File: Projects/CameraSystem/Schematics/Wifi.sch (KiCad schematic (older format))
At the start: 0 parts

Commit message: wifi module added
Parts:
- added C?: 100n, symbol Device:C
- added R?: 10k, symbol Device:R
- added U?: ESP8266, symbol cl-integrated_circuits:ESP8266
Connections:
- new net GND: C?.2, U?.1 (GND)
- new net VDD_3V3: C?.1, R?.1, U?.8 (3.3V)
- new net WIFI_EN: R?.2, U?.4 (CHEN)
- new net WIFI_RST: U?.6 (RST)
- new net WIFI_RX: U?.7 (RXI)
- new net WIFI_TX: U?.2 (TXO)
- no-connect marks 0 -> 2
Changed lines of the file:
@@
 Comment4 ""
 $EndDescr
+$Comp
+L cl-integrated_circuits:ESP8266 U?
+U 1 1 5CA59F23
+P 3450 2550
+F 0 "U?" H 3450 2987 60  0000 C CNN
+F 1 "ESP8266" H 3450 2881 60  0000 C CNN
+F 2 "" H 3450 2550 60  0001 C CNN
+F 3 "" H 3450 2550 60  0001 C CNN
+	1    3450 2550
+	1    0    0    -1
+$EndComp
+Text HLabel 4750 2700 2    50   Input ~ 0
+WIFI_RX
+Text HLabel 2450 2400 0    50   Output ~ 0
+WIFI_TX
+Text HLabel 2450 2700 0    50   Input ~ 0
+VDD_3V3
+Wire Wire Line
+	2450 2700 2750 2700
+Wire Wire Line
+	2950 2600 2450 2600
+Text HLabel 2450 2600 0    50   Input ~ 0
+WIFI_RST
+$Comp
+L power:GND #PWR?
+U 1 1 5CA5A1DA
+P 4700 2400
+F 0 "#PWR?" H 4700 2150 50  0001 C CNN
+F 1 "GND" V 4705 2272 50  0000 R CNN
+F 2 "" H 4700 2400 50  0001 C CNN
+F 3 "" H 4700 2400 50  0001 C CNN
+	1    4700 2400
+	0    -1   -1   0
+$EndComp
+Wire Wire Line
+	3950 2400 4700 2400
+Wire Wire Line
+	3950 2700 4750 2700
+Wire Wire Line
+	2450 2400 2950 2400
+NoConn ~ 3950 2500
+NoConn ~ 3950 2600
+Wire Wire Line
+	2950 2500 1900 2500
+Text HLabel 1750 2500 0    50   Input ~ 0
+WIFI_EN
+$Comp
+L Device:R R?
+U 1 1 5CA5A6FA
+P 1900 2200
+F 0 "R?" H 1970 2246 50  0000 L CNN
+F 1 "10k" H 1970 2155 50  0000 L CNN
+F 2 "" V 1830 2200 50  0001 C CNN
+F 3 "~" H 1900 2200 50  0001 C CNN
+	1    1900 2200
+	1    0    0    -1
+$EndComp
+Wire Wire Line
+	1900 2350 1900 2500
+Connection ~ 1900 2500
+Wire Wire Line
+	1900 2500 1750 2500
+Wire Wire Line
+	1900 2050 1900 1850
+Text Label 1900 1850 0    50   ~ 0
+VDD_3V3
+$Comp
+L Device:C C?
+U 1 1 5CA5ADFE
+P 2750 3000
+F 0 "C?" H 2865 3046 50  0000 L CNN
+F 1 "100n" H 2865 2955 50  0000 L CNN
+F 2 "" H 2788 2850 50  0001 C CNN
+F 3 "~" H 2750 3000 50  0001 C CNN
+	1    2750 3000
+	1    0    0    -1
+$EndComp
+Wire Wire Line
+	2750 2700 2750 2850
+Connection ~ 2750 2700
+Wire Wire Line
+	2750 2700 2950 2700
+Wire Wire Line
+	2750 3150 2750 3300
+$Comp
+L power:GND #PWR?
+U 1 1 5CA5AF47
+P 2750 3300
+F 0 "#PWR?" H 2750 3050 50  0001 C CNN
+F 1 "GND" H 2755 3127 50  0000 C CNN
+F 2 "" H 2750 3300 50  0001 C CNN
+F 3 "" H 2750 3300 50  0001 C CNN
+	1    2750 3300
+	1    0    0    -1
+$EndComp
 $EndSCHEMATC

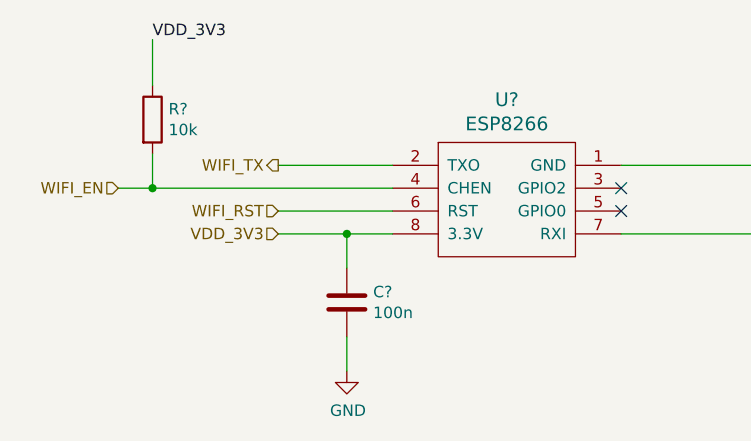
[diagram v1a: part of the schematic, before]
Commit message: wifi module added
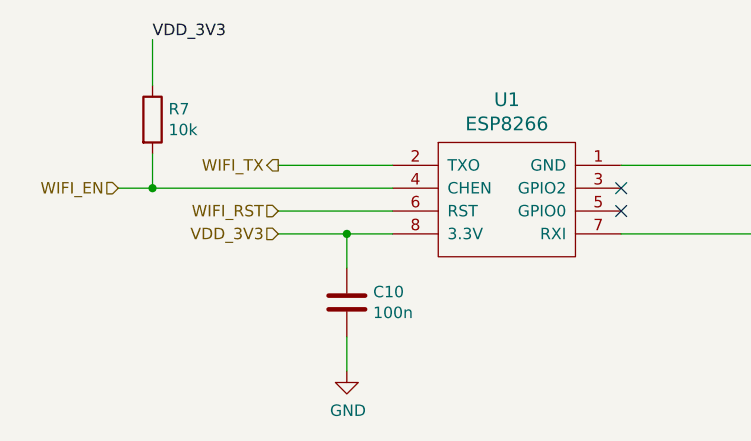
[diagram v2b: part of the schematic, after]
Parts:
- gave numbers to parts that had none: 3
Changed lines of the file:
@@
 $EndDescr
 $Comp
-L cl-integrated_circuits:ESP8266 U?
+L cl-integrated_circuits:ESP8266 U1
 U 1 1 5CA59F23
 P 3450 2550
-F 0 "U?" H 3450 2987 60  0000 C CNN
+F 0 "U1" H 3450 2987 60  0000 C CNN
 F 1 "ESP8266" H 3450 2881 60  0000 C CNN
 F 2 "" H 3450 2550 60  0001 C CNN
@@
 WIFI_RST
 $Comp
-L power:GND #PWR?
+L power:GND #PWR09
 U 1 1 5CA5A1DA
 P 4700 2400
-F 0 "#PWR?" H 4700 2150 50  0001 C CNN
+F 0 "#PWR09" H 4700 2150 50  0001 C CNN
 F 1 "GND" V 4705 2272 50  0000 R CNN
 F 2 "" H 4700 2400 50  0001 C CNN
@@
 WIFI_EN
 $Comp
-L Device:R R?
+L Device:R R7
 U 1 1 5CA5A6FA
 P 1900 2200
-F 0 "R?" H 1970 2246 50  0000 L CNN
+F 0 "R7" H 1970 2246 50  0000 L CNN
 F 1 "10k" H 1970 2155 50  0000 L CNN
 F 2 "" V 1830 2200 50  0001 C CNN
@@
 VDD_3V3
 $Comp
-L Device:C C?
+L Device:C C10
 U 1 1 5CA5ADFE
 P 2750 3000
-F 0 "C?" H 2865 3046 50  0000 L CNN
+F 0 "C10" H 2865 3046 50  0000 L CNN
 F 1 "100n" H 2865 2955 50  0000 L CNN
 F 2 "" H 2788 2850 50  0001 C CNN
@@
 	2750 3150 2750 3300
 $Comp
-L power:GND #PWR?
+L power:GND #PWR08
 U 1 1 5CA5AF47
 P 2750 3300
-F 0 "#PWR?" H 2750 3050 50  0001 C CNN
+F 0 "#PWR08" H 2750 3050 50  0001 C CNN
 F 1 "GND" H 2755 3127 50  0000 C CNN
 F 2 "" H 2750 3300 50  0001 C CNN

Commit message: camera was updated
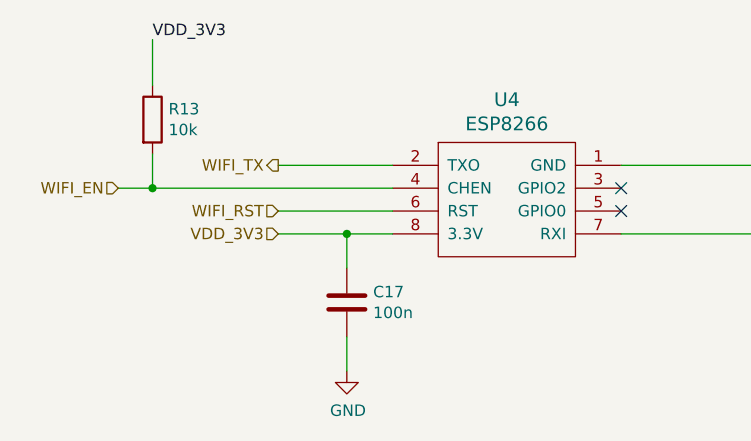
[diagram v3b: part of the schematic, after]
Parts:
- C17: renamed from C10; footprint (none) -> Capacitor_SMD:C_0603_1608Metric_Pad1.05x0.95mm_HandSolder
- R13: renamed from R7; footprint (none) -> Resistor_SMD:R_0603_1608Metric_Pad1.05x0.95mm_HandSolder
- U4: renamed from U1; footprint (none) -> Connector_PinSocket_2.54mm:PinSocket_2x04_P2.54mm_Vertical
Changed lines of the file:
@@
 EESchema Schematic File Version 4
 LIBS:CameraSystem-cache
-EELAYER 26 0
+EELAYER 29 0
 EELAYER END
 $Descr A4 11693 8268
@@
 $EndDescr
 $Comp
-L cl-integrated_circuits:ESP8266 U1
+L cl-integrated_circuits:ESP8266 U4
 U 1 1 5CA59F23
 P 3450 2550
-F 0 "U1" H 3450 2987 60  0000 C CNN
+F 0 "U4" H 3450 2987 60  0000 C CNN
 F 1 "ESP8266" H 3450 2881 60  0000 C CNN
-F 2 "" H 3450 2550 60  0001 C CNN
+F 2 "Connector_PinSocket_2.54mm:PinSocket_2x04_P2.54mm_Vertical" H 3450 2550 60  0001 C CNN
 F 3 "" H 3450 2550 60  0001 C CNN
 	1    3450 2550
@@
 WIFI_RST
 $Comp
-L power:GND #PWR09
+L power:GND #PWR024
 U 1 1 5CA5A1DA
 P 4700 2400
-F 0 "#PWR09" H 4700 2150 50  0001 C CNN
+F 0 "#PWR024" H 4700 2150 50  0001 C CNN
 F 1 "GND" V 4705 2272 50  0000 R CNN
 F 2 "" H 4700 2400 50  0001 C CNN
@@
 WIFI_EN
 $Comp
-L Device:R R7
+L Device:R R13
 U 1 1 5CA5A6FA
 P 1900 2200
-F 0 "R7" H 1970 2246 50  0000 L CNN
+F 0 "R13" H 1970 2246 50  0000 L CNN
 F 1 "10k" H 1970 2155 50  0000 L CNN
-F 2 "" V 1830 2200 50  0001 C CNN
+F 2 "Resistor_SMD:R_0603_1608Metric_Pad1.05x0.95mm_HandSolder" V 1830 2200 50  0001 C CNN
 F 3 "~" H 1900 2200 50  0001 C CNN
 	1    1900 2200
@@
 VDD_3V3
 $Comp
-L Device:C C10
+L Device:C C17
 U 1 1 5CA5ADFE
 P 2750 3000
-F 0 "C10" H 2865 3046 50  0000 L CNN
+F 0 "C17" H 2865 3046 50  0000 L CNN
 F 1 "100n" H 2865 2955 50  0000 L CNN
-F 2 "" H 2788 2850 50  0001 C CNN
+F 2 "Capacitor_SMD:C_0603_1608Metric_Pad1.05x0.95mm_HandSolder" H 2788 2850 50  0001 C CNN
 F 3 "~" H 2750 3000 50  0001 C CNN
 	1    2750 3000
@@
 	2750 3150 2750 3300
 $Comp
-L power:GND #PWR08
+L power:GND #PWR023
 U 1 1 5CA5AF47
 P 2750 3300
-F 0 "#PWR08" H 2750 3050 50  0001 C CNN
+F 0 "#PWR023" H 2750 3050 50  0001 C CNN
 F 1 "GND" H 2755 3127 50  0000 C CNN
 F 2 "" H 2750 3300 50  0001 C CNN

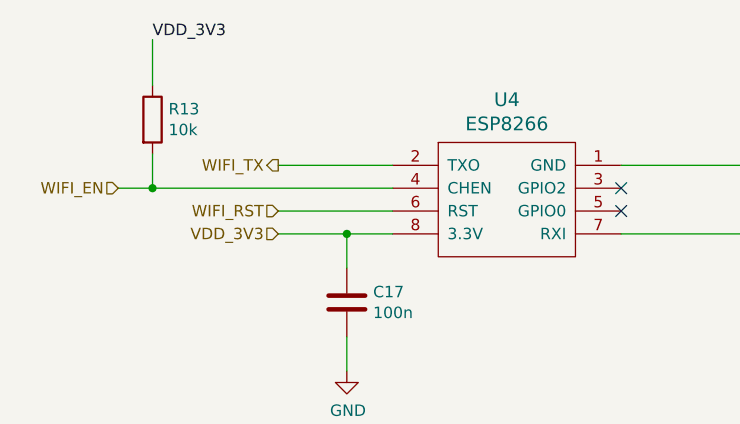
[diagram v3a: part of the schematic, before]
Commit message: camera was updated
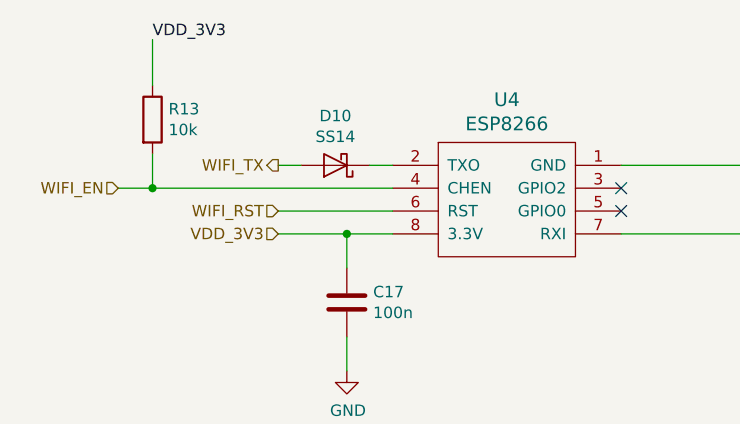
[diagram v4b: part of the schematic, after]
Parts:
- added D10: SS14, custom-footprints:SMA_DO-214AC, symbol Device:D_Schottky
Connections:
- net WIFI_TX: now also D10.2 (A); no longer U4.2 (TXO)
- new net: D10.1 (K), U4.2 (TXO)
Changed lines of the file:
@@
 	3950 2700 4750 2700
 Wire Wire Line
-	2450 2400 2950 2400
+	2450 2400 2550 2400
 NoConn ~ 3950 2500
 NoConn ~ 3950 2600
@@
 	1    0    0    -1
 $EndComp
+$Comp
+L Device:D_Schottky D10
+U 1 1 5CAE8217
+P 2700 2400
+F 0 "D10" H 2700 2184 50  0000 C CNN
+F 1 "SS14" H 2700 2275 50  0000 C CNN
+F 2 "custom-footprints:SMA_DO-214AC" H 2700 2400 50  0001 C CNN
+F 3 "~" H 2700 2400 50  0001 C CNN
+	1    2700 2400
+	-1   0    0    1
+$EndComp
+Wire Wire Line
+	2850 2400 2950 2400
 $EndSCHEMATC

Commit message: nothing hcanged
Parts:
- removed C17: 100n, Capacitor_SMD:C_0603_1608Metric_Pad1.05x0.95mm_HandSolder, symbol Device:C
- removed D10: SS14, custom-footprints:SMA_DO-214AC, symbol Device:D_Schottky
- removed R13: 10k, Resistor_SMD:R_0603_1608Metric_Pad1.05x0.95mm_HandSolder, symbol Device:R
- added C18: 100n, digikey-footprints:0603, symbol Device:C
- added J6: Conn_02x02_Odd_Even, Pin_Headers:Pin_Header_Straight_2x02_Pitch2.54mm_SMD, symbol Connector_Generic:Conn_02x02_Odd_Even
- added Q1: BC846B_215, digikey-footprints:SOT-23-3, symbol CameraSystem-rescue:BC846B_215
- added R22: 4K7, digikey-footprints:0603, symbol Device:R
- added R23, R24: 10k, digikey-footprints:0603, symbol Device:R
- U4: footprint Connector_PinSocket_2.54mm:PinSocket_2x04_P2.54mm_Vertical -> Pin_Headers:Pin_Header_Straight_2x04_Pitch2.54mm
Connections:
- net GND: now also C18.2, Q1.2 (E), R23.1
- net VDD_3V3: now also J6.1 (Pin_1), J6.3 (Pin_3); no longer U4.8 (3.3V)
- net WIFI_RST: now also R22.2; no longer U4.6 (RST)
- net WIFI_TX: now also U4.2 (TXO)
- new net: Q1.3 (C), R24.1, U4.6 (RST)
- new net: Q1.1 (B), R22.1, R23.2
- new net VDD_3V3_IN: C18.1, J6.2 (Pin_2), J6.4 (Pin_4), R24.2, U4.8 (3.3V)
